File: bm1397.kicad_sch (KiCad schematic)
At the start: 55 parts, among them IC1 BM1397_mode1, J3 Conn_01x05, U1 25MHz, U2 LN1134A182MR-G, U3 SN74AXC1T45DBVR, U4 SGM2036-ADJYN5G/TR

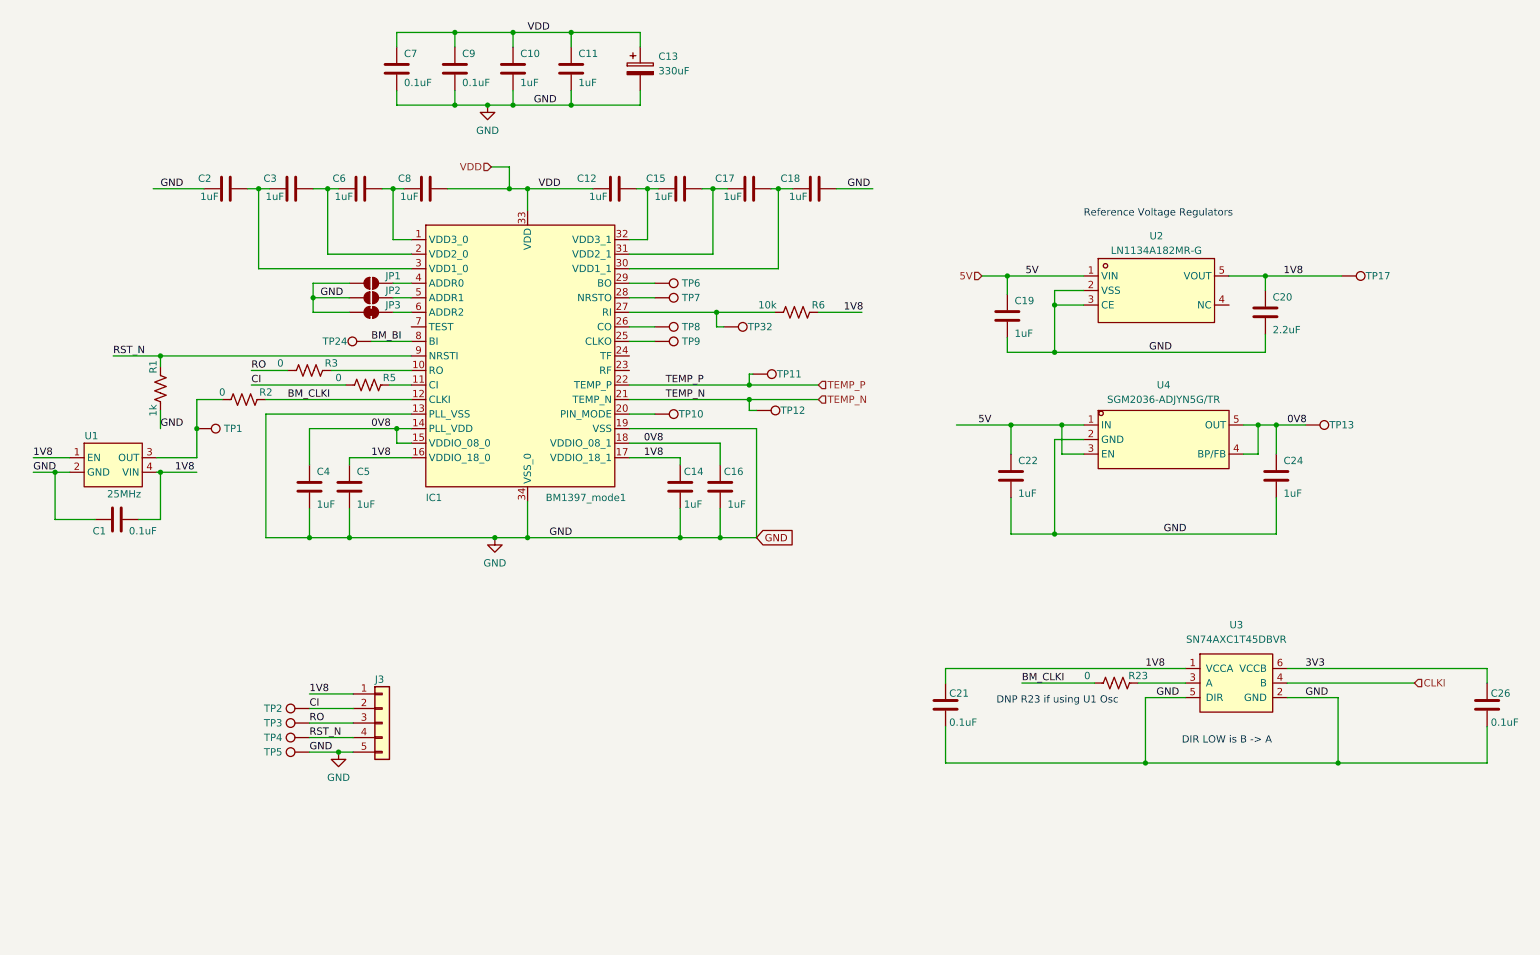
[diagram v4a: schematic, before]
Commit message: added 4 discrete level shifters with LCSC stock
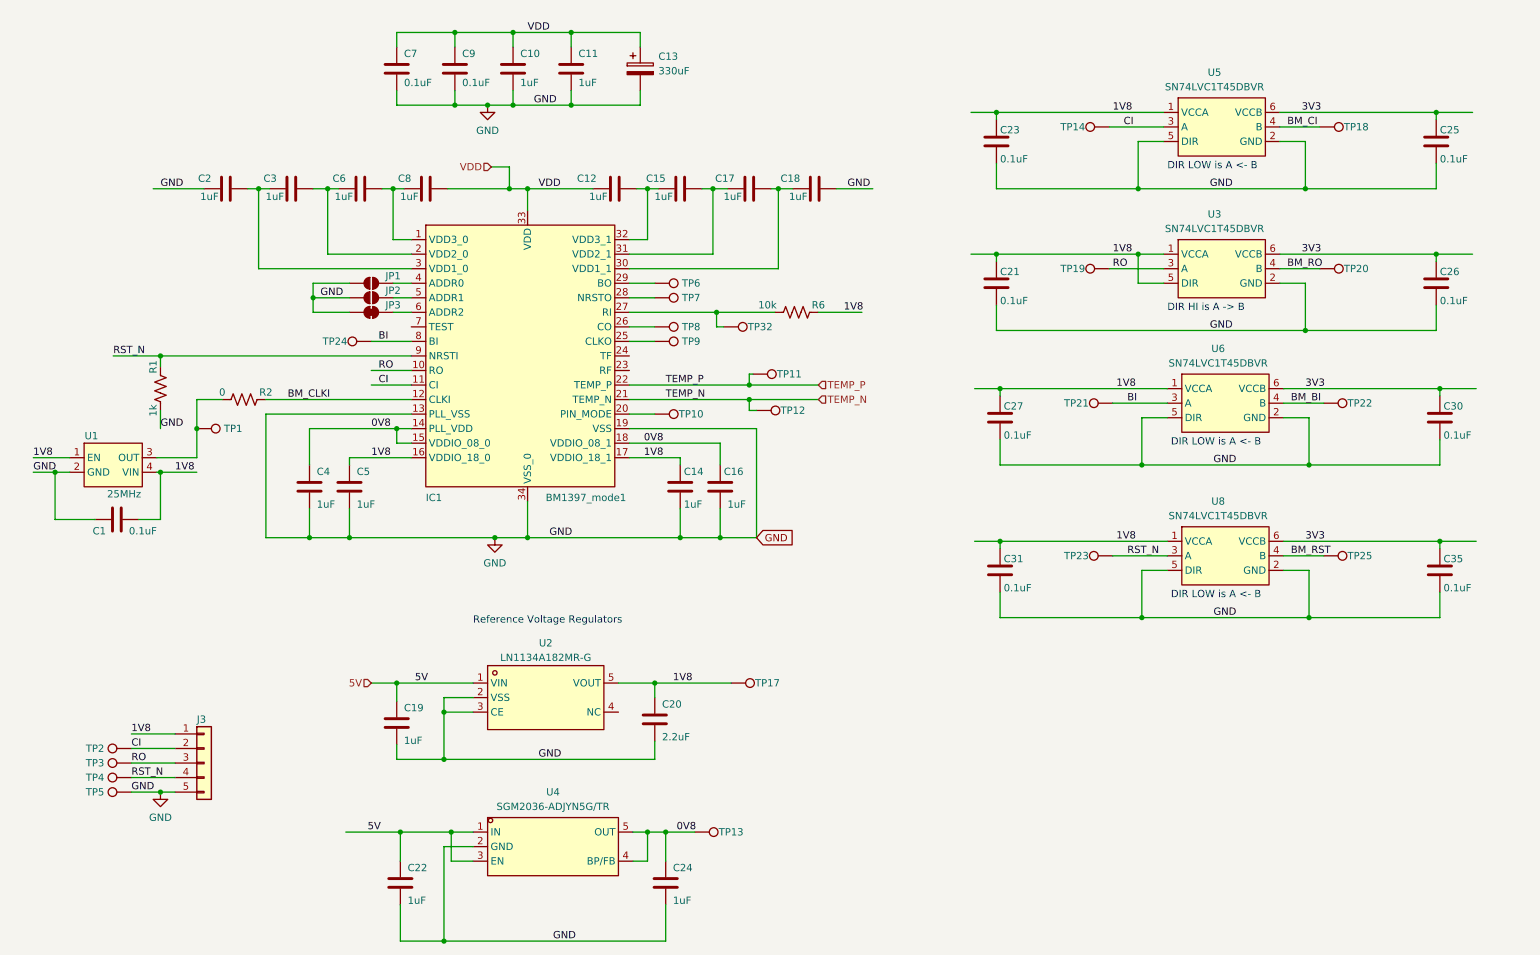
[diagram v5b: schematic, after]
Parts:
- removed R23, R3, R5: 0, Resistor_SMD:R_0402_1005Metric, symbol Device:R_US
- removed U3: SN74AXC1T45DBVR, bitaxe:SN74AXC1T45, symbol bitaxe:SN74AXC1T45DBVR
- added C23, C25, C27, C30, C31, C35: 311-3342-1-ND, Capacitor_SMD:C_0402_1005Metric, symbol Device:C
- added TP14, TP18, TP19, TP20, TP21, TP22, TP23, TP25: TestPoint, TestPoint:TestPoint_Pad_D1.5mm, symbol Connector:TestPoint
- added U3, U5, U6, U8: SN74LVC1T45DBVR, lcsc:SOT-23-6_L2.9-W1.6-P0.95-LS2.8-BR, symbol lcsc:SN74LVC1T45DBVR
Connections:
- net 1V8: now also C23.1, C27.1, C31.1, U3.1 (VCCA), U3.5 (DIR), U5.1 (VCCA), U6.1 (VCCA), U8.1 (VCCA)
- net 3V3: now also C25.1, C30.1, C35.1, U3.6 (VCCB), U5.6 (VCCB), U6.6 (VCCB), U8.6 (VCCB)
- net BM_BI: now also TP22.1, U6.4 (B); no longer IC1.8 (BI), TP24.1
- net CI: now also IC1.11 (CI), TP14.1, U5.3 (A)
- net GND: now also C23.2, C25.2, C27.2, C30.2, C31.2, C35.2, U3.2 (GND), U5.2 (GND), U5.5 (DIR), U6.2 (GND), U6.5 (DIR), U8.2 (GND), U8.5 (DIR)
- net RO: now also IC1.10 (RO), TP19.1, U3.3 (A)
- net RST_N: now also TP23.1, U8.3 (A)
- new net BI: IC1.8 (BI), TP21.1, TP24.1, U6.3 (A)
- new net BM_CI: TP18.1, U5.4 (B)
- new net BM_RO: TP20.1, U3.4 (B)
- new net BM_RST: TP25.1, U8.4 (B)
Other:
- note added: "DIR HI is A -> B"
- note added: "DIR LOW is A <- B"
- note removed: "DIR LOW is B -> A"
- note removed: "DNP R23 if using U1 Osc"
- moved on the sheet: C19, C20, C22, C24, J3, TP13, TP17, TP2, TP3, TP4, TP5, U2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

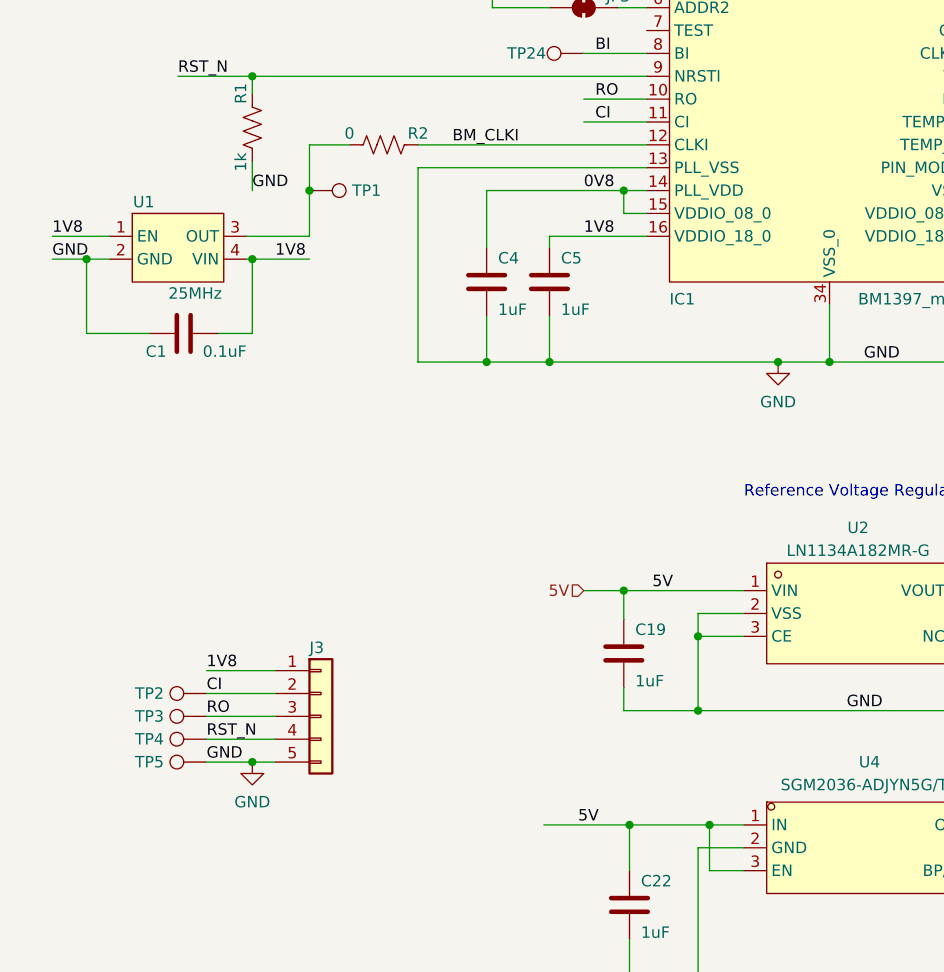
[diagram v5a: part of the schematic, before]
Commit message: swapped 25MHz Osc for LCSC model
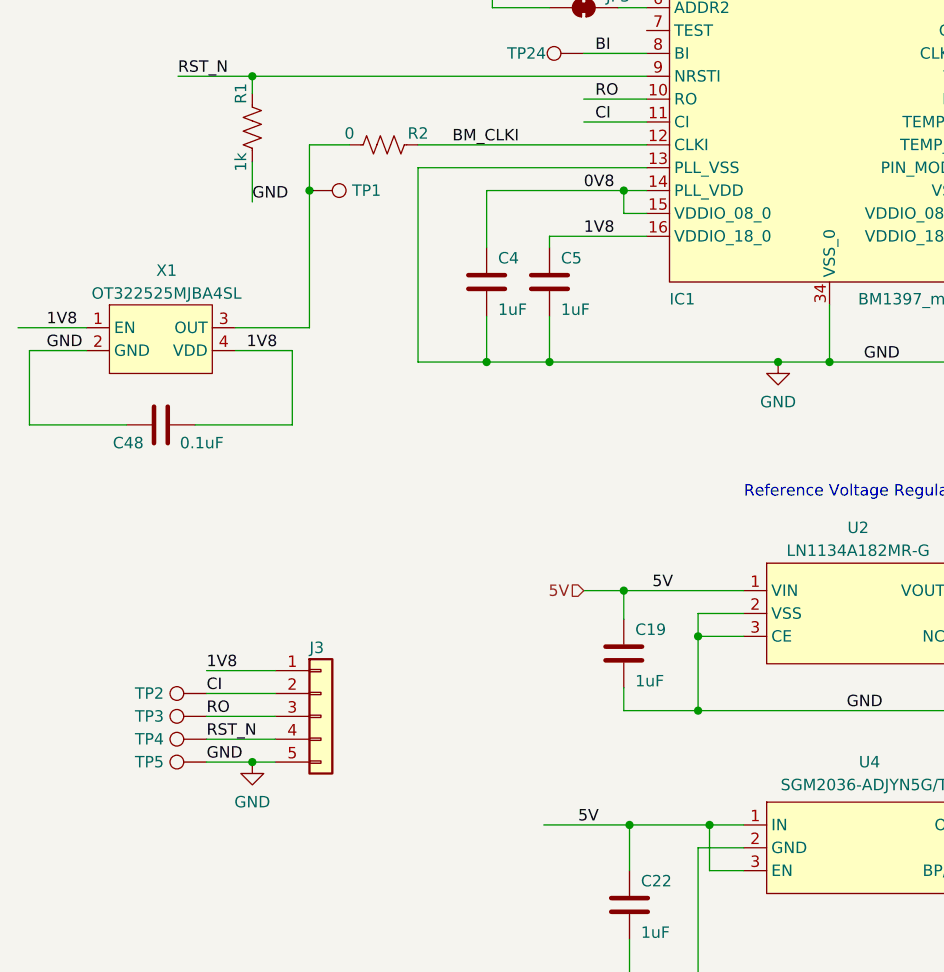
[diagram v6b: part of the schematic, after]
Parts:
- removed C1: 311-3342-1-ND, Capacitor_SMD:C_0402_1005Metric, symbol Device:C
- removed U1: 25MHz, bitaxe:O 25,0-JO32-B-1V3-1-T1-LF, symbol bitaxe:oscillator
- added C48: 311-3342-1-ND, Capacitor_SMD:C_0402_1005Metric, symbol Device:C
- added X1: OT322525MJBA4SL, lcsc:OSC-SMD_4P-L3.2-W2.5-BL, symbol lcsc:OT322525MJBA4SL
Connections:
- net 1V8: now also C48.2, X1.1 (EN), X1.4 (VDD)
- net GND: now also C48.1, X1.2 (GND)
- net at R2.1, TP1.1: now also X1.3 (OUT)

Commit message: cleanup. added LCSC fan connector
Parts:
- removed R2: 0, Resistor_SMD:R_0402_1005Metric, symbol Device:R_US
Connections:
- net BM_CLKI is gone; now on an unnamed net: IC1.12 (CLKI)
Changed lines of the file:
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@@
     (stroke (width 0) (type default))
   )
-  (wire (pts (xy 48.26 92.71) (xy 52.705 92.71))
-    (stroke (width 0) (type default))
-  )
   (wire (pts (xy 217.805 95.885) (xy 213.36 95.885))
     (stroke (width 0) (type default))
@@
     (stroke (width 0) (type default))
   )
-  (wire (pts (xy 60.325 92.71) (xy 85.725 92.71))
+  (wire (pts (xy 48.26 92.71) (xy 85.725 92.71))
     (stroke (width 0) (type default))
   )
@@
     (effects (font (size 1.27 1.27)) (justify left bottom))
   )
-  (label "BM_CLKI" (at 64.135 92.71 0) (fields_autoplaced)
-    (effects (font (size 1.27 1.27)) (justify left bottom))
-  )
   (label "RST_N" (at 33.655 85.09 0) (fields_autoplaced)
     (effects (font (size 1.27 1.27)) (justify left bottom))
@@
         )
       )
-    )
-  )
-  (symbol (lib_id "Device:R_US") (at 56.515 92.71 90) (unit 1)
-    (in_bom yes) (on_board yes) (dnp no)
-    (property "Reference" "R2" (at 60.325 91.44 90)
-      (effects (font (size 1.27 1.27)))
-    )
-    (property "Value" "0" (at 52.705 91.44 90)
-      (effects (font (size 1.27 1.27)))
-    )
-    (property "Footprint" "Resistor_SMD:R_0402_1005Metric" (at 56.769 91.694 90)
-      (effects (font (size 1.27 1.27)) hide)
-    )
-    (property "Datasheet" "~" (at 56.515 92.71 0)
-      (effects (font (size 1.27 1.27)) hide)
-    )
-    (property "DK" "RMCF0402ZT0R00CT-ND" (at 56.515 92.71 0)
-      (effects (font (size 1.27 1.27)) hide)
-    )
-    (property "PARTNO" "RMCF0402ZT0R00" (at 56.515 92.71 0)
-      (effects (font (size 1.27 1.27)) hide)
-    )
-    (pin "1")
-    (pin "2")
-    (instances
-      (project "Hashat"
-        (path "/00740941-7ad8-466a-a267-188591e2b5c4/5aa25910-cf6c-433c-86f8-40d28be84b47"
-          (reference "R2") (unit 1)
-        )
-      )
-      (project "bitaxeMax"
-        (path "/e63e39d7-6ac0-4ffd-8aa3-1841a4541b55/4cf9c075-d009-4c35-9949-adda70ae20c7"
-          (reference "R2") (unit 1)
-        )
-      )

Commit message: started on new LM5085 based buck design
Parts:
- C19, C22, C24: DK (none) -> 587-5514-1-ND; PARTNO (none) -> EMK105BJ105MV-F
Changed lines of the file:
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@@
       (effects (font (size 1.27 1.27)) hide)
     )
-    (property "DK" "" (at 83.185 149.225 0)
-      (effects (font (size 1.778 1.5113)) (justify left bottom) hide)
-    )
-    (property "PARTNO" "" (at 83.185 149.225 0)
+    (property "DK" "587-5514-1-ND" (at 83.185 149.225 0)
+      (effects (font (size 1.778 1.5113)) (justify left bottom) hide)
+    )
+    (property "PARTNO" "EMK105BJ105MV-F" (at 83.185 149.225 0)
       (effects (font (size 1.27 1.27)) hide)
     )
@@
       (effects (font (size 1.27 1.27)) hide)
     )
-    (property "DK" "" (at 130.175 177.165 0)
-      (effects (font (size 1.778 1.5113)) (justify left bottom) hide)
-    )
-    (property "PARTNO" "" (at 130.175 177.165 0)
+    (property "DK" "587-5514-1-ND" (at 130.175 177.165 0)
+      (effects (font (size 1.778 1.5113)) (justify left bottom) hide)
+    )
+    (property "PARTNO" "EMK105BJ105MV-F" (at 130.175 177.165 0)
       (effects (font (size 1.27 1.27)) hide)
     )
@@
       (effects (font (size 1.27 1.27)) hide)
     )
-    (property "DK" "" (at 83.82 177.165 0)
-      (effects (font (size 1.778 1.5113)) (justify left bottom) hide)
-    )
-    (property "PARTNO" "" (at 83.82 177.165 0)
-      (effects (font (size 1.27 1.27)) hide)
-    )
+    (property "DK" "587-5514-1-ND" (at 83.82 177.165 0)
+      (effects (font (size 1.778 1.5113)) (justify left bottom) hide)
+    )
+    (property "PARTNO" "EMK105BJ105MV-F" (at 83.82 177.165 0)
+      (effects (font (size 1.27 1.27)) hide)
+    )
